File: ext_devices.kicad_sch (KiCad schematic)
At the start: 24 parts, among them CON1 MIKROBUS_HOST_CONN, J14 Conn_01x08_Socket, J15 Conn_01x08_Socket, U12 TXS0102DCU, U13 TXS0102DCU, U16 SN74LV1T34DBV, U17 SN74LV1T34DBV, U18 SN74LV1T34DBV, U19 SN74LV1T34DBV, U20 SN74LV1T34DBV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

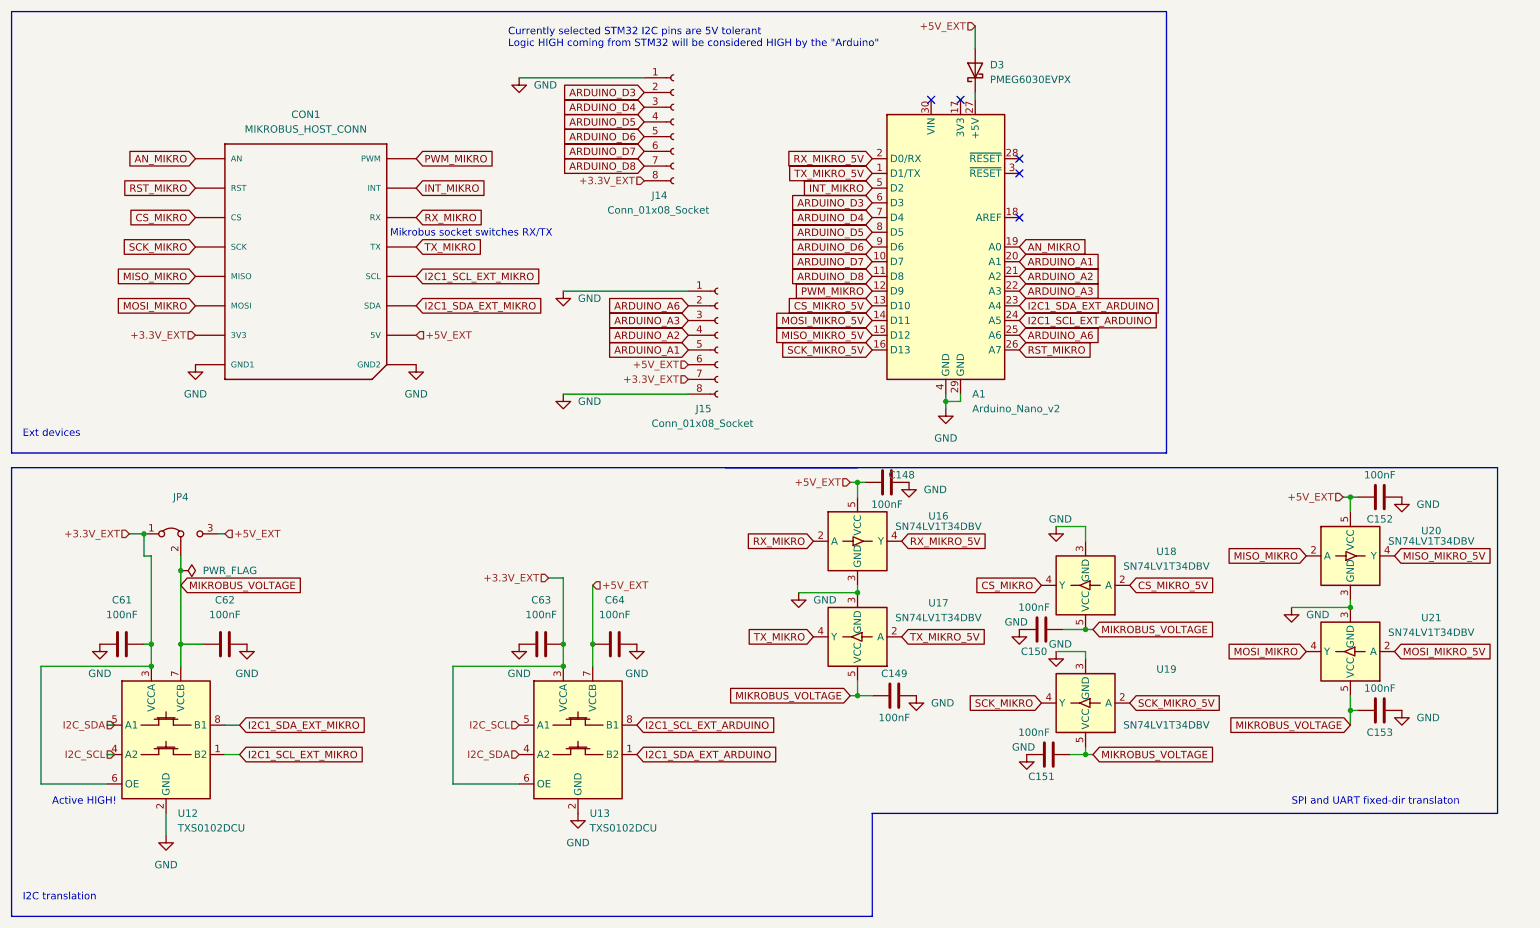
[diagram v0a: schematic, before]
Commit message: removed resistors from rotary enc;  aligned mikrobus socket to the center
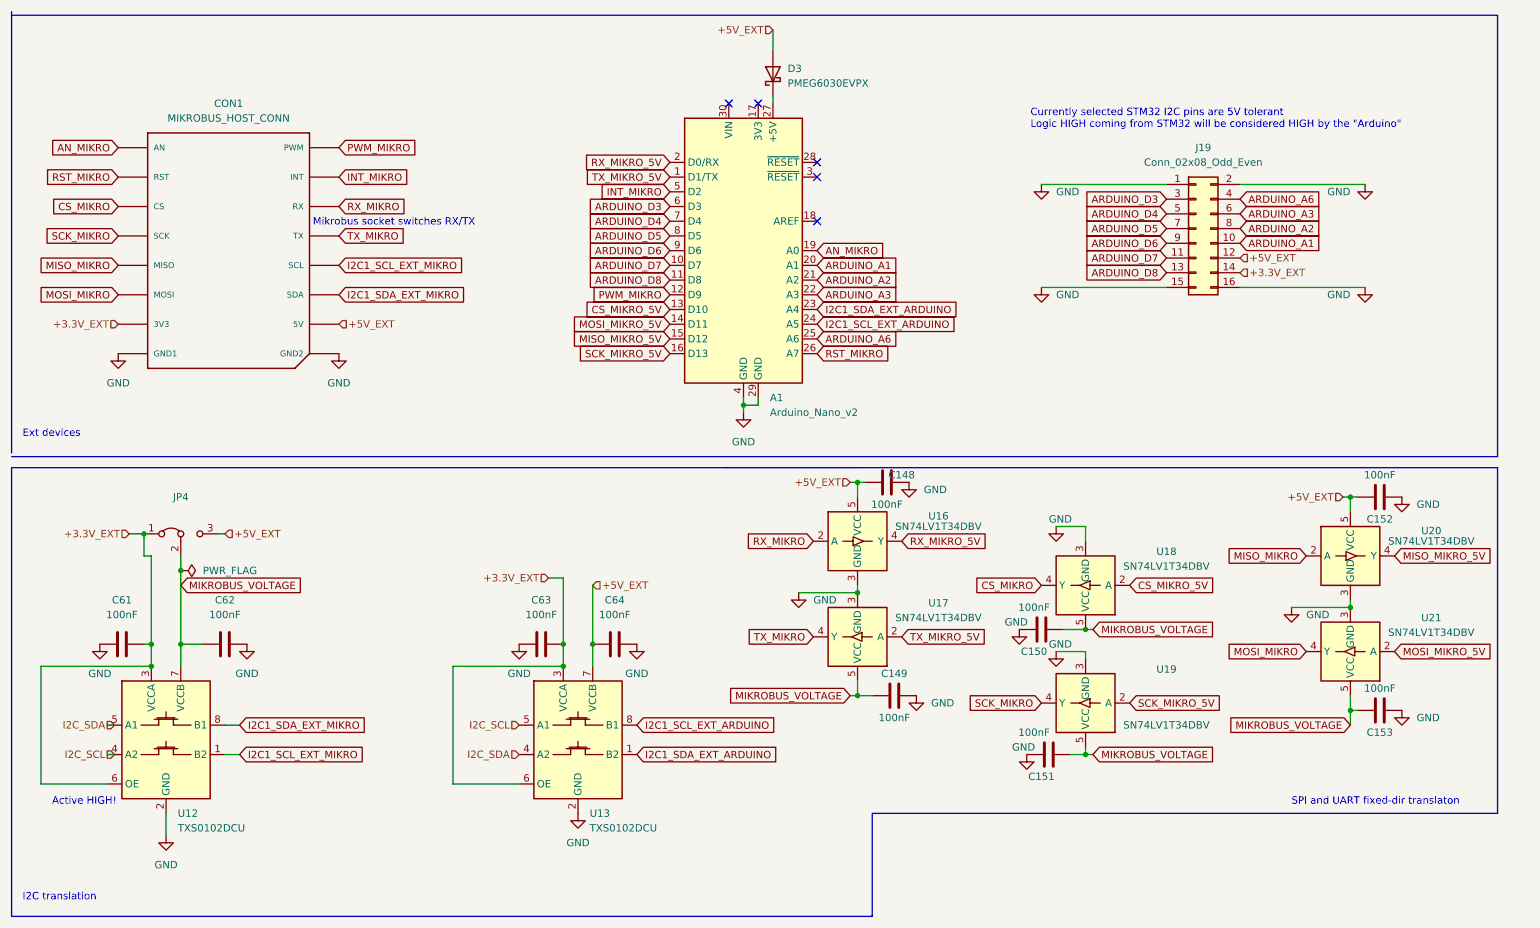
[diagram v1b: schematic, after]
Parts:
- removed J14, J15: Conn_01x08_Socket, Connector_PinSocket_2.54mm:PinSocket_1x08_P2.54mm_Vertical, symbol Connector:Conn_01x08_Socket
- added J19: Conn_02x08_Odd_Even, Connector_PinSocket_2.54mm:PinSocket_2x08_P2.54mm_Vertical, symbol Connector_Generic:Conn_02x08_Odd_Even
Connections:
- net +3.3V_EXT: now also J19.14 (Pin_14)
- net +5V_EXT: now also J19.12 (Pin_12)
- net ARDUINO_A1: now also J19.10 (Pin_10)
- net ARDUINO_A2: now also J19.8 (Pin_8)
- net ARDUINO_A3: now also J19.6 (Pin_6)
- net ARDUINO_A6: now also J19.4 (Pin_4)
- net ARDUINO_D3: now also J19.3 (Pin_3)
- net ARDUINO_D4: now also J19.5 (Pin_5)
- net ARDUINO_D5: now also J19.7 (Pin_7)
- net ARDUINO_D6: now also J19.9 (Pin_9)
- net ARDUINO_D7: now also J19.11 (Pin_11)
- net ARDUINO_D8: now also J19.13 (Pin_13)
- net GND: now also J19.1 (Pin_1), J19.15 (Pin_15), J19.16 (Pin_16), J19.2 (Pin_2)
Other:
- moved on the sheet: A1, CON1, D3

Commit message: updating Robotont library footprint assignments in schematics; connected usb-c connector's mounting holes to ground planes
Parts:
- A1: footprint Module:Arduino_Nano -> Robotont:Arduino_Nano
- D3: footprint Diode_SMD:D_SOD-128 -> Robotont:D_SOD-128
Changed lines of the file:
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@@
       (effects (font (size 1.27 1.27)) (justify left))
     )
-    (property "Footprint" "Module:Arduino_Nano" (at 153.035 67.945 0)
+    (property "Footprint" "Robotont:Arduino_Nano" (at 153.035 67.945 0)
       (effects (font (size 1.27 1.27) italic) hide)
     )
@@
       (effects (font (size 1.27 1.27)) (justify right))
     )
-    (property "Footprint" "Diode_SMD:D_SOD-128" (at 158.115 37.465 0)
-      (effects (font (size 1.27 1.27)) hide)
-    )
+    (property "Footprint" "Robotont:D_SOD-128" (at 158.115 37.465 0)
+      (effects (font (size 1.27 1.27)) hide)
+    )

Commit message: fixed i2c3_sda pin (from PA9 to PC9), excluding manual asm components from bom
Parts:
- A1, CON1, J19, JP4: now left out of the parts list
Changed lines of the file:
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@@
   )
   (symbol (lib_id "Jumper:Jumper_3_Bridged12") (at 55.88 116.84 0) (unit 1)
-    (in_bom yes) (on_board yes) (dnp no)
+    (in_bom no) (on_board yes) (dnp no)
     (property "Reference" "JP4" (at 55.88 110.49 0)
       (effects (font (size 1.27 1.27)))
@@
   )
   (symbol (lib_id "MCU_Module:Arduino_Nano_v2.x") (at 153.035 67.945 0) (unit 1)
-    (in_bom yes) (on_board yes) (dnp no) (fields_autoplaced)
+    (in_bom no) (on_board yes) (dnp no) (fields_autoplaced)
     (property "Reference" "A1" (at 157.5944 93.345 0)
       (effects (font (size 1.27 1.27)) (justify left))
@@
   )
   (symbol (lib_id "Robotont:MIKROBUS_HOST_CONN") (at 50.165 88.265 0) (unit 1)
-    (in_bom yes) (on_board yes) (dnp no) (fields_autoplaced)
+    (in_bom no) (on_board yes) (dnp no) (fields_autoplaced)
     (property "Reference" "CON1" (at 64.135 42.545 0)
       (effects (font (size 1.27 1.27)))
@@
   )
   (symbol (lib_id "Connector_Generic:Conn_02x08_Odd_Even") (at 231.14 64.135 0) (unit 1)
-    (in_bom yes) (on_board yes) (dnp no) (fields_autoplaced)
+    (in_bom no) (on_board yes) (dnp no) (fields_autoplaced)
     (property "Reference" "J19" (at 232.41 50.165 0)
       (effects (font (size 1.27 1.27)))

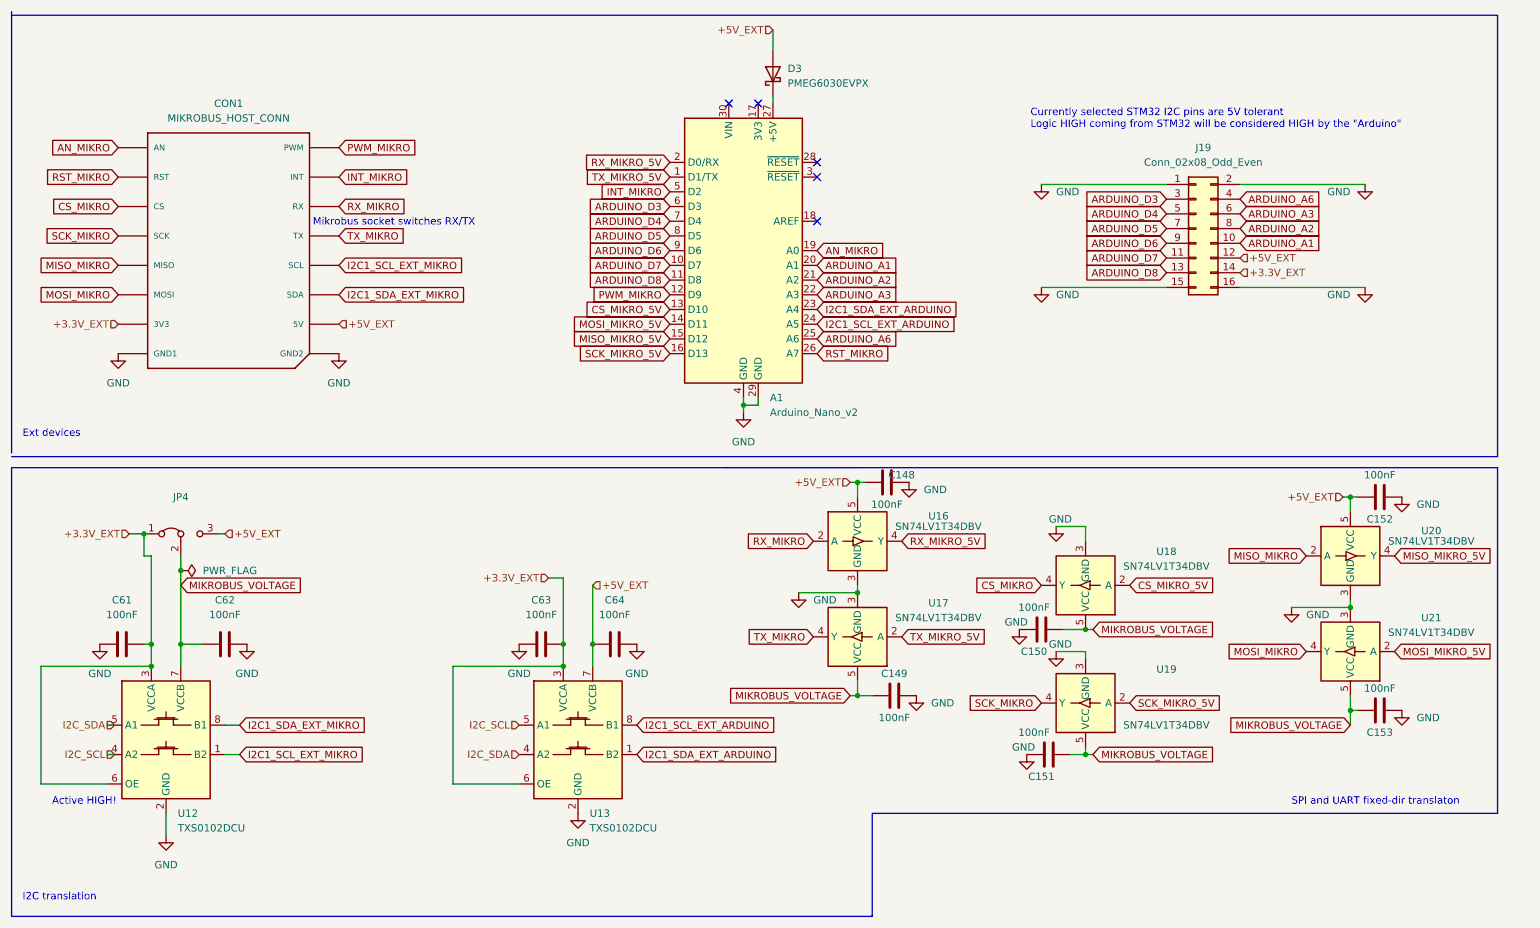
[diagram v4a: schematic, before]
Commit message: setting 'do not populate' attribute for manually assembled components
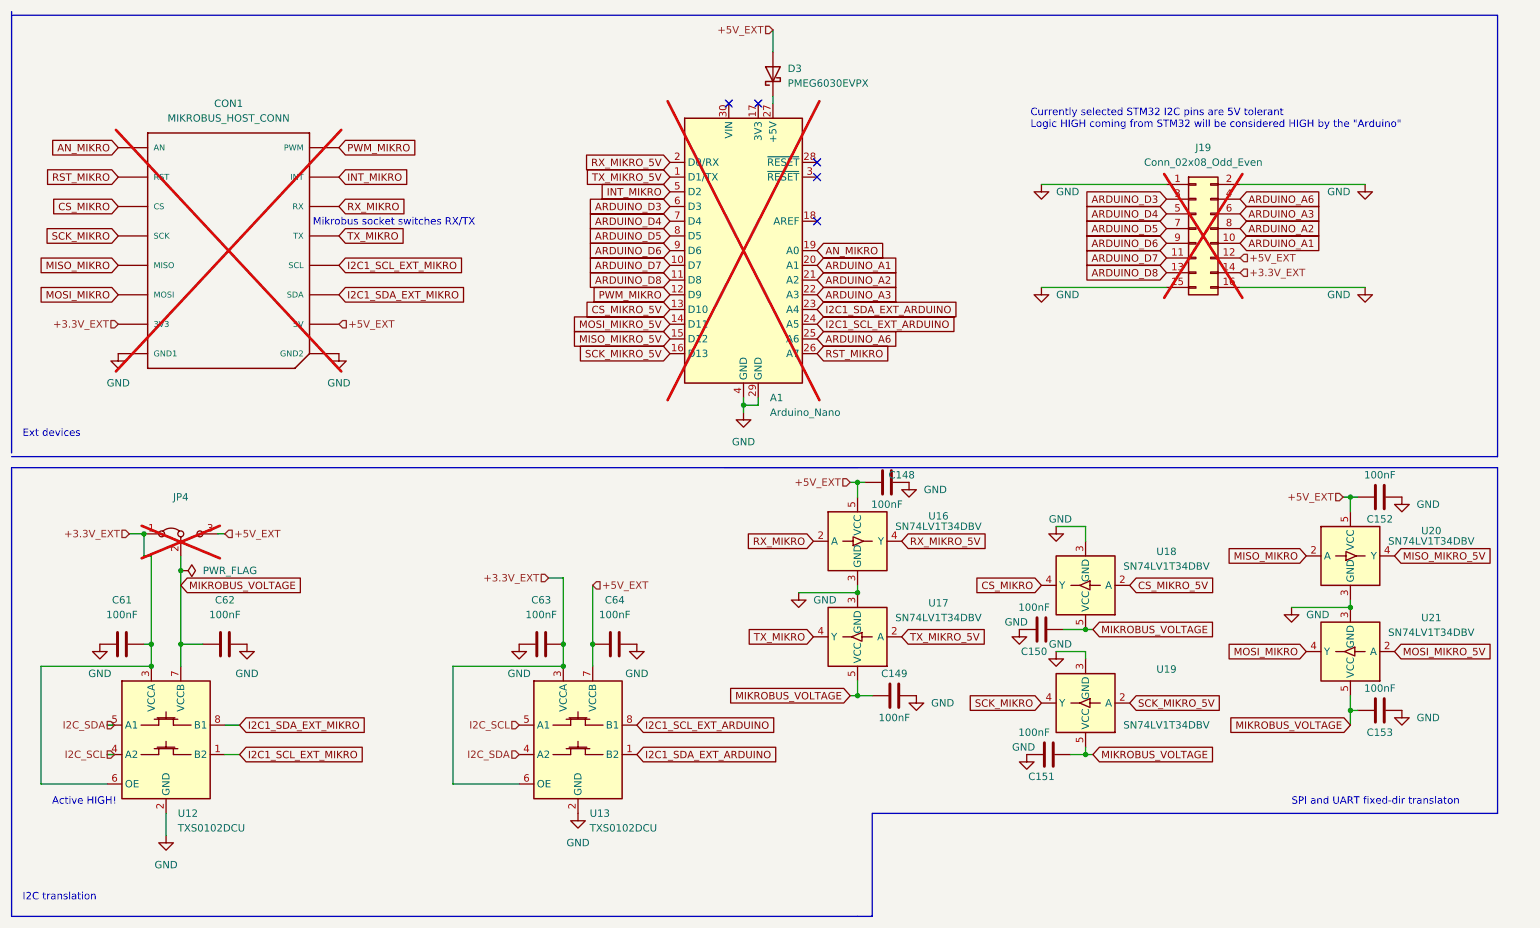
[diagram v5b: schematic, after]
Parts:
- A1: value Arduino_Nano_v2 -> Arduino_Nano; now not fitted; now in the parts list
- CON1, J19, JP4: now not fitted; now in the parts list
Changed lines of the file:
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@@
   )
   (symbol (lib_id "Jumper:Jumper_3_Bridged12") (at 55.88 116.84 0) (unit 1)
-    (in_bom no) (on_board yes) (dnp no)
+    (in_bom yes) (on_board yes) (dnp yes)
     (property "Reference" "JP4" (at 55.88 110.49 0)
       (effects (font (size 1.27 1.27)))
@@
   )
   (symbol (lib_id "MCU_Module:Arduino_Nano_v2.x") (at 153.035 67.945 0) (unit 1)
-    (in_bom no) (on_board yes) (dnp no) (fields_autoplaced)
+    (in_bom yes) (on_board yes) (dnp yes) (fields_autoplaced)
     (property "Reference" "A1" (at 157.5944 93.345 0)
       (effects (font (size 1.27 1.27)) (justify left))
     )
-    (property "Value" "Arduino_Nano_v2" (at 157.5944 95.885 0)
+    (property "Value" "Arduino_Nano" (at 157.5944 95.885 0)
       (effects (font (size 1.27 1.27)) (justify left))
     )
@@
   )
   (symbol (lib_id "Robotont:MIKROBUS_HOST_CONN") (at 50.165 88.265 0) (unit 1)
-    (in_bom no) (on_board yes) (dnp no) (fields_autoplaced)
+    (in_bom yes) (on_board yes) (dnp yes) (fields_autoplaced)
     (property "Reference" "CON1" (at 64.135 42.545 0)
       (effects (font (size 1.27 1.27)))
@@
   )
   (symbol (lib_id "Connector_Generic:Conn_02x08_Odd_Even") (at 231.14 64.135 0) (unit 1)
-    (in_bom no) (on_board yes) (dnp no) (fields_autoplaced)
+    (in_bom yes) (on_board yes) (dnp yes) (fields_autoplaced)
     (property "Reference" "J19" (at 232.41 50.165 0)
       (effects (font (size 1.27 1.27)))

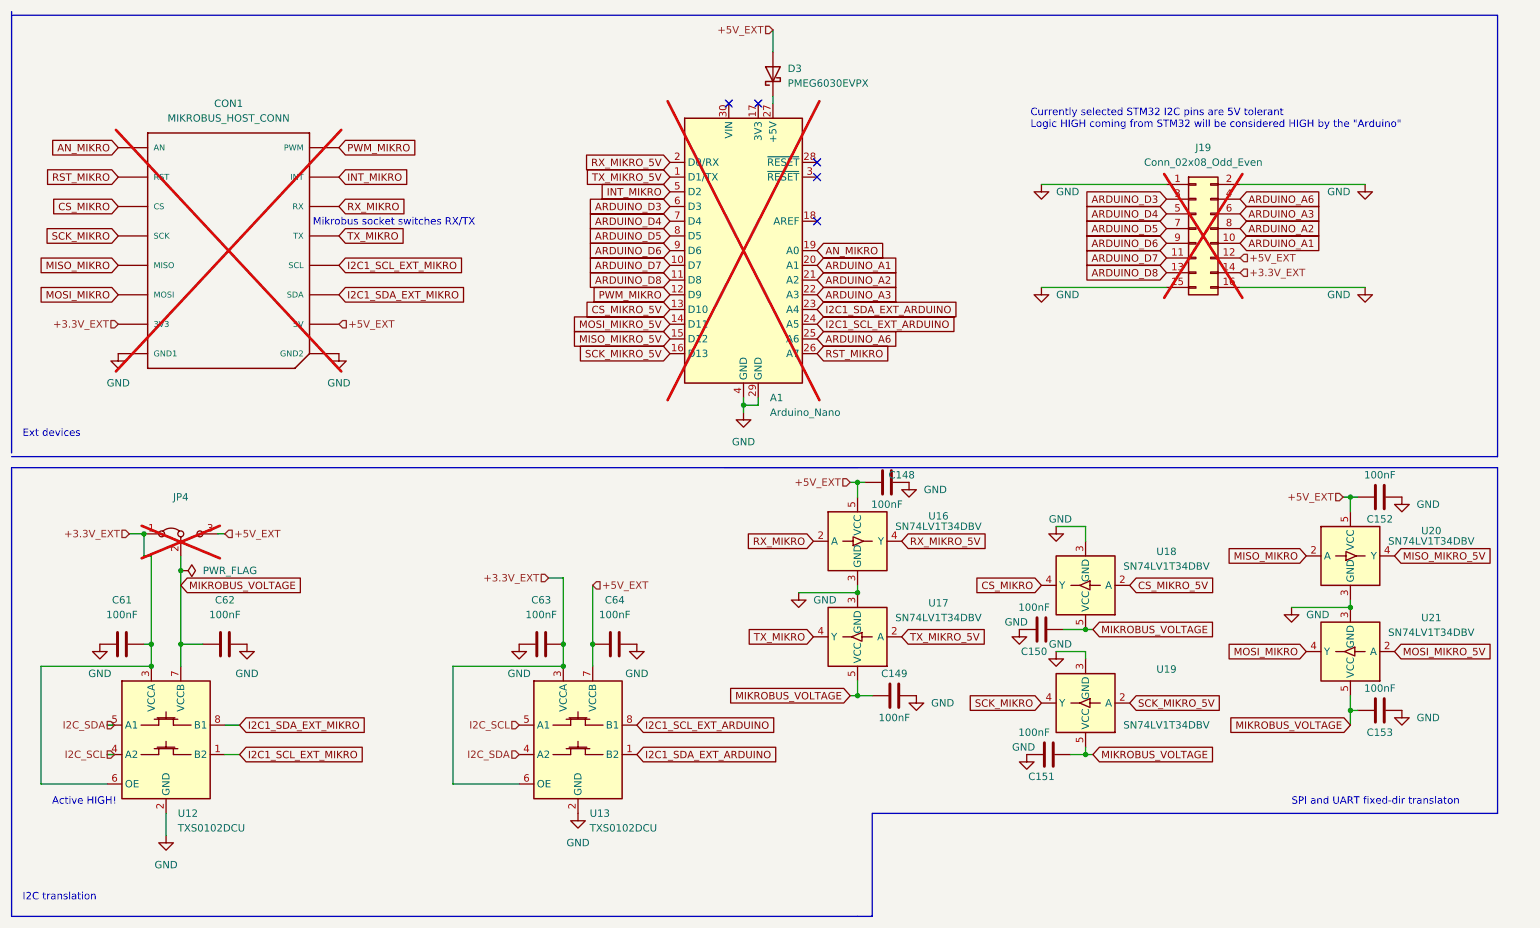
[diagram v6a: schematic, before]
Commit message: updated to kicad 9, added comparator-based power source switching
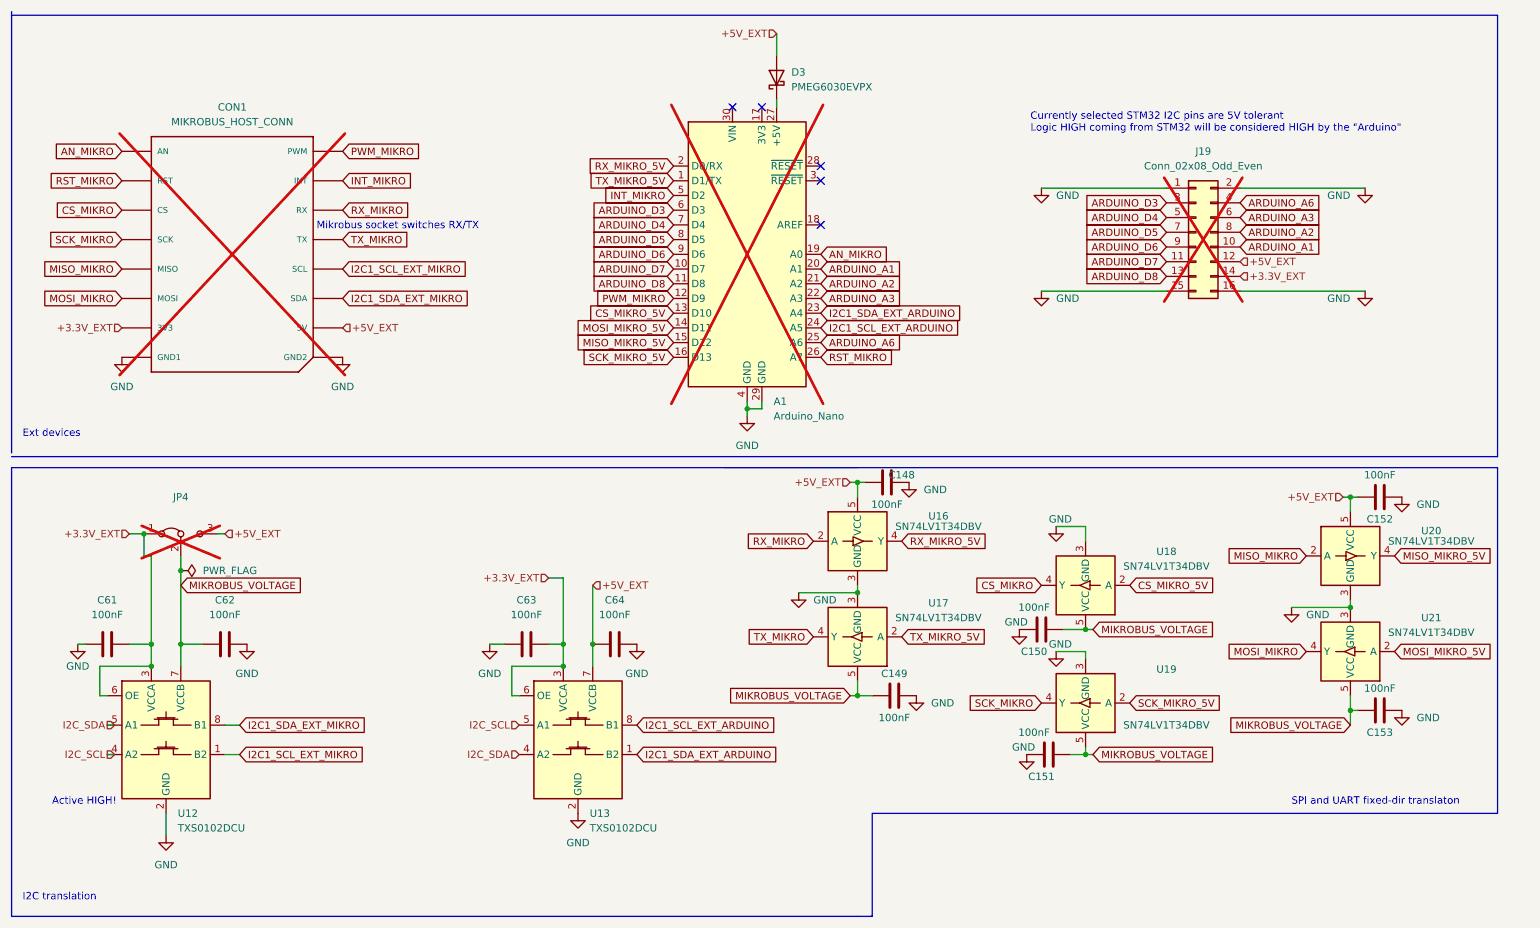
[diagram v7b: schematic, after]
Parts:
- JP4: value (none) -> ~
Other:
- moved on the sheet: A1, C61, C63, CON1, D3, J19
